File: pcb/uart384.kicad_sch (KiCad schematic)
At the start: 37 parts, among them IC1 ICE40LP384-SG32, J1 USB_A, J2 TC2050, J3 Conn_02x07_Odd_Even, J4 TC2050_ext, SW1 SW_Push, U1 AT25DF256-SSHN, U2 CP2102-QFN28, U3 MIC5365-1.2YC5, Y1 XO32

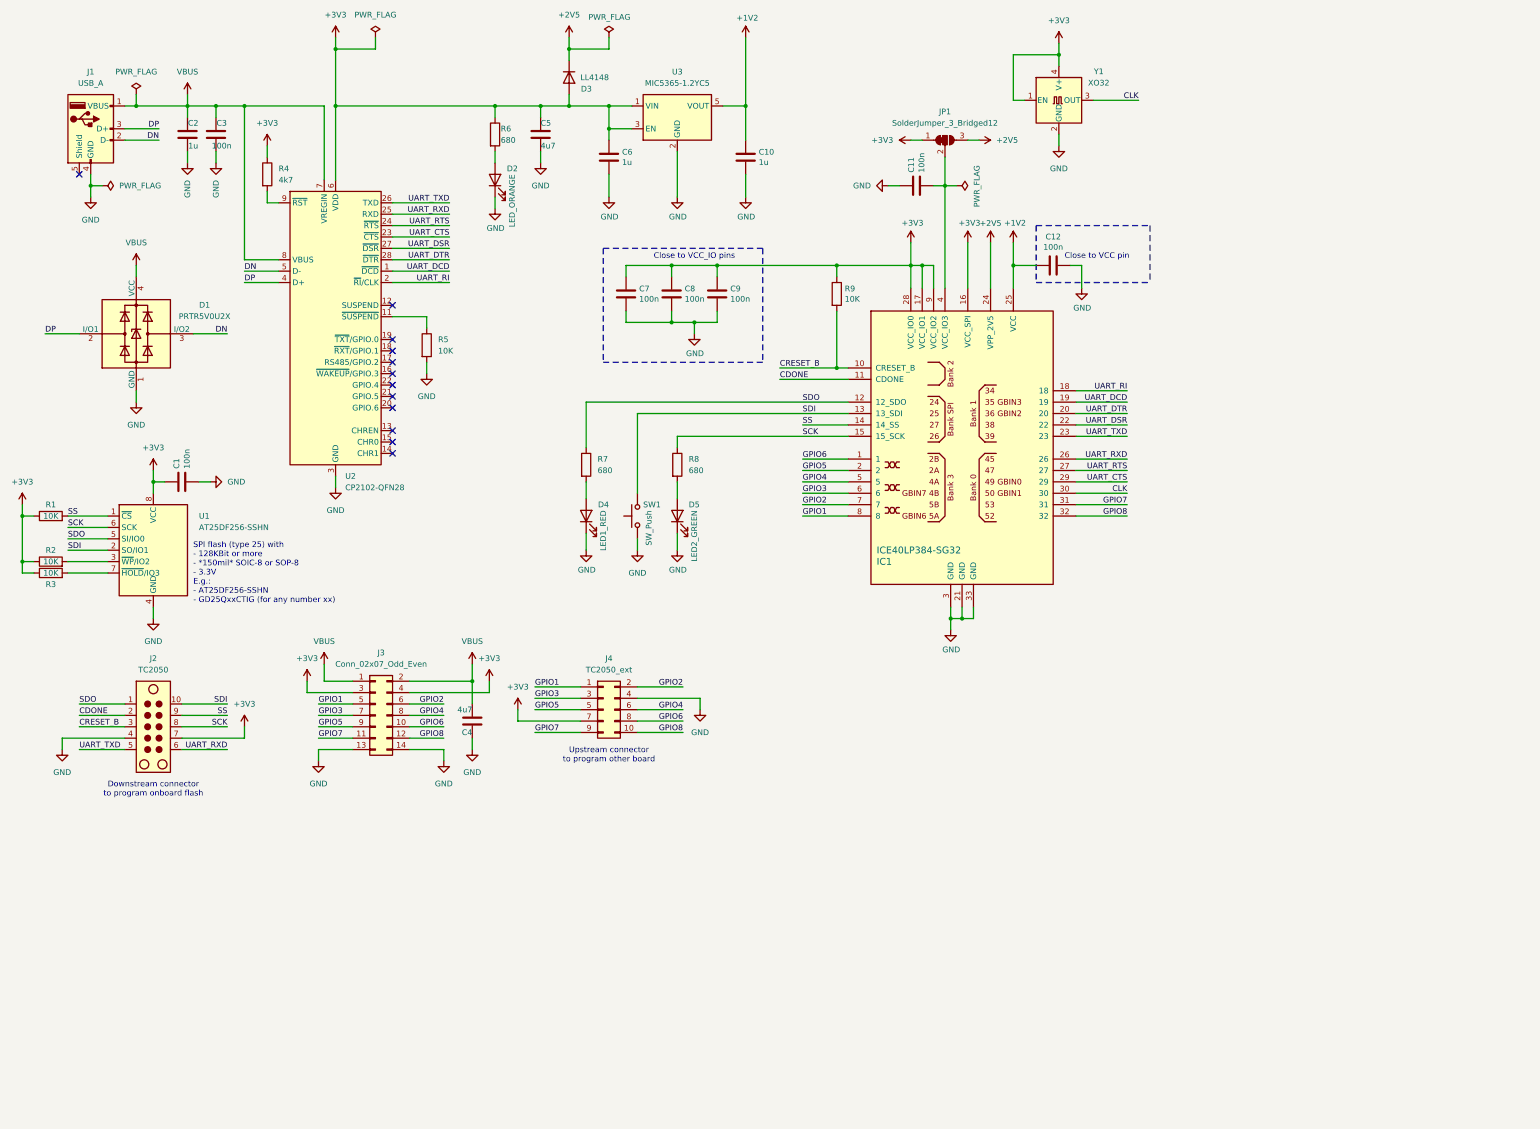
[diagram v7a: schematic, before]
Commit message: PCB: add voltage regulator choices for VCC_IO3, selectable via jumper, DNP
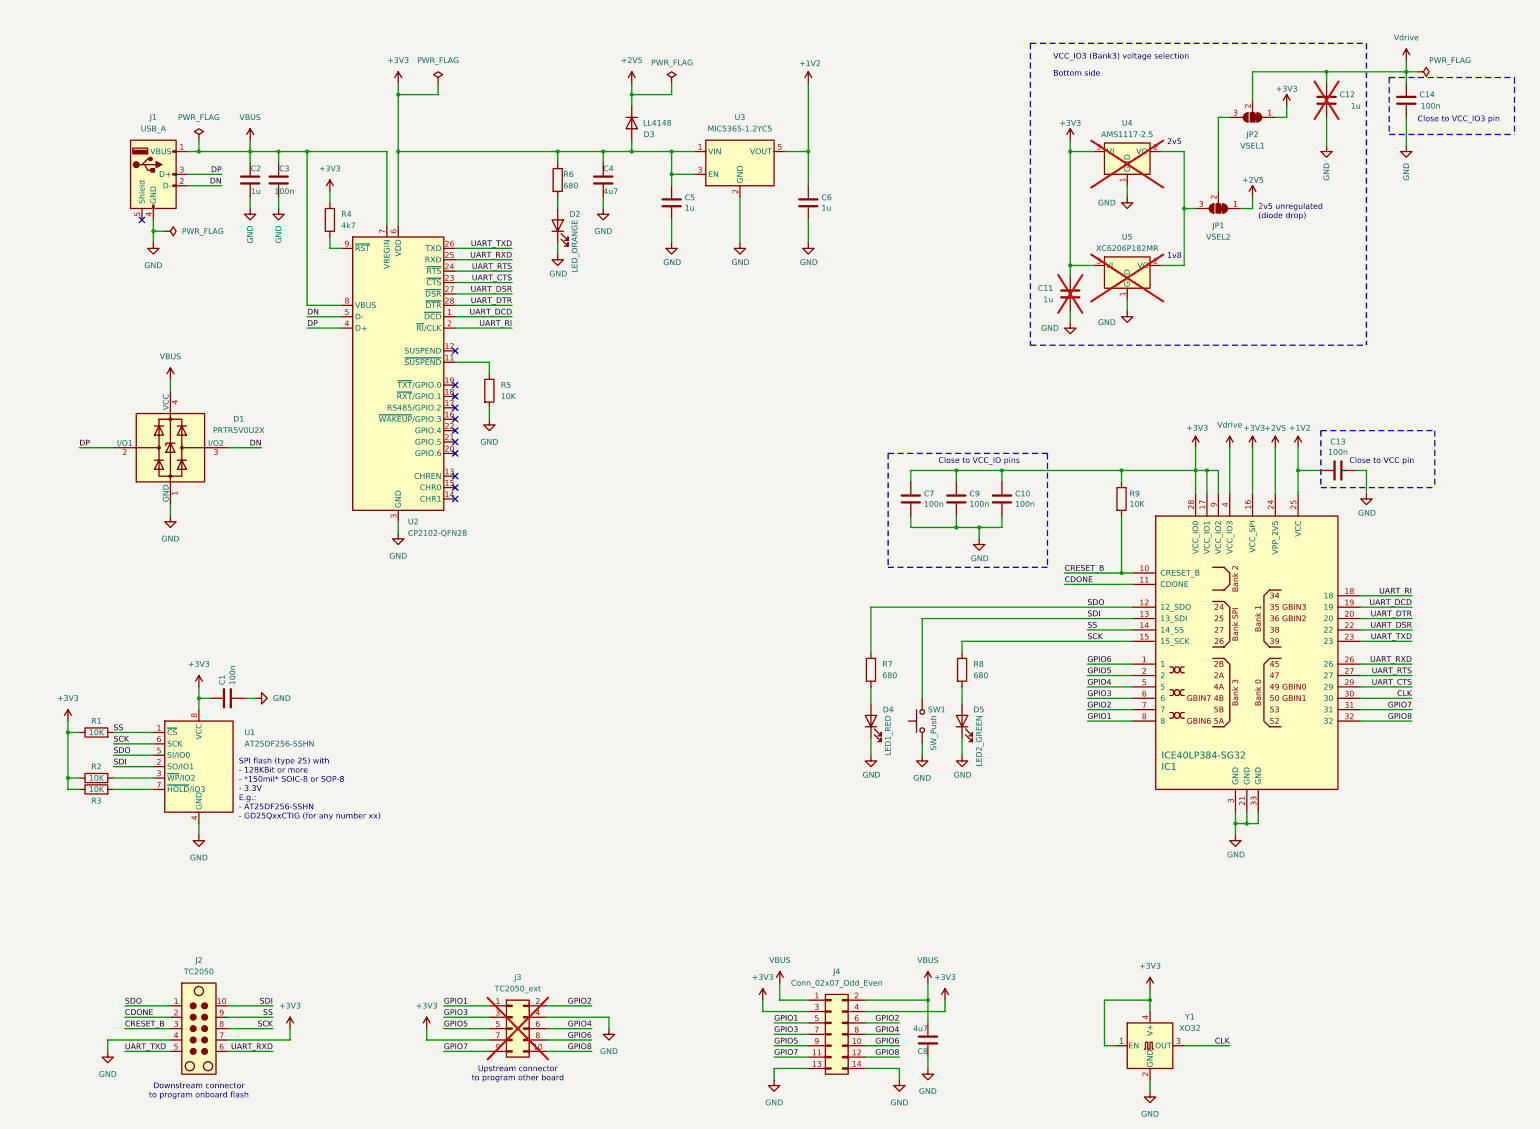
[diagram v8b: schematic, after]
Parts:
- added C11, C12: 1u, Capacitor_SMD:C_0603_1608Metric, symbol Device:C
- added JP1: VSEL2, Jumper:SolderJumper-3_P1.3mm_Bridged2Bar12_RoundedPad1.0x1.5mm, symbol Jumper:SolderJumper_3_Bridged12
- added U4: AMS1117-2.5, Package_TO_SOT_SMD:SOT-223-3_TabPin2, symbol Regulator_Linear:AMS1117-2.5
- added U5: XC6206P182MR, Package_TO_SOT_SMD:SOT-23-3, symbol Regulator_Linear:XC6206PxxxMR
- J3: renamed from J4; now not fitted
- JP2: renamed from JP1; value SolderJumper_3_Bridged12 -> VSEL1
- renumbered C9 to C10, C12 to C13, C11 to C14, C5 to C4, C6 to C5, C10 to C6, C4 to C8, C8 to C9, J3 to J4
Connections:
- net +2V5: now also JP1.1 (A); no longer JP2.3 (B)
- net +3V3: now also C11.2, U4.3 (VI), U5.3 (VI)
- net GND: now also C11.1, C12.1, U4.1 (GND), U5.1 (GND)
- net Vdrive: now reaches C14.2, IC1.4 (VCC_IO3), JP2.2 (C)
- net Vdrive: now also C12.2
- new net: JP1.3 (B), U4.2 (VO), U5.2 (VO)
- new net: JP1.2 (C), JP2.3 (B)
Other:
- note added: "1v8"
- note added: "2v5"
- note added: "2v5 unregulated (diode drop)"
- note added: "Bottom side"
- note added: "Close to VCC_IO3 pin"
- note added: "VCC_IO3 (Bank3) voltage selection"
- moved on the sheet: C1, C10, C13, C14, C2, C3, C4, C5, C6, C7, C8, C9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
